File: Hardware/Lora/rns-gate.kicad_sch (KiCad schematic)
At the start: 2 parts, among them J2 Conn_02x13_Odd_Even, U1 E22-900M30S-SX1262

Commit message: Update Lora module
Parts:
- added C1: C_Polarized_Small, Capacitor_Tantalum_SMD:CP_EIA-7343-43_Kemet-X_Pad2.25x2.55mm_HandSolder, symbol Device:C_Polarized_Small
- added C2, C3: C_Small, Capacitor_SMD:C_0805_2012Metric_Pad1.18x1.45mm_HandSolder, symbol Device:C_Small
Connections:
- net +5V: now also C1.1, C2.1, C3.1
- net GND: now also C1.2, C2.2, C3.2
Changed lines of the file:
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@@
 (kicad_sch (version 20211123) (generator eeschema)
   (paper "A4")
+  (junction (at 144.78 159.004) (diameter 0) (color 0 0 0 0)
+  )
+  (junction (at 144.78 169.418) (diameter 0) (color 0 0 0 0)
+  )
+  (junction (at 152.654 159.004) (diameter 0) (color 0 0 0 0)
+  )
   (junction (at 160.02 144.018) (diameter 0) (color 0 0 0 0)
+  )
+  (junction (at 152.654 169.418) (diameter 0) (color 0 0 0 0)
   )
   (no_connect (at 106.172 119.888))
@@
   (no_connect (at 163.576 116.078))
   (no_connect (at 163.576 136.398))
+  (wire (pts (xy 144.78 169.418) (xy 152.654 169.418))
+    (stroke (width 0) (type default) (color 0 0 0 0))
+  )
   (wire (pts (xy 176.276 138.938) (xy 182.372 138.938))
     (stroke (width 0) (type default) (color 0 0 0 0))
   )
+  (wire (pts (xy 161.29 166.37) (xy 161.29 169.418))
+    (stroke (width 0) (type default) (color 0 0 0 0))
+  )
   (wire (pts (xy 156.718 128.778) (xy 163.576 128.778))
     (stroke (width 0) (type default) (color 0 0 0 0))
@@
     (stroke (width 0) (type default) (color 0 0 0 0))
   )
+  (wire (pts (xy 152.654 159.004) (xy 161.29 159.004))
+    (stroke (width 0) (type default) (color 0 0 0 0))
+  )
+  (wire (pts (xy 144.78 159.004) (xy 144.78 161.29))
+    (stroke (width 0) (type default) (color 0 0 0 0))
+  )
   (wire (pts (xy 176.276 121.158) (xy 181.61 121.158))
     (stroke (width 0) (type default) (color 0 0 0 0))
@@
     (stroke (width 0) (type default) (color 0 0 0 0))
   )
+  (wire (pts (xy 144.78 156.972) (xy 144.78 159.004))
+    (stroke (width 0) (type default) (color 0 0 0 0))
+  )
   (wire (pts (xy 155.448 141.478) (xy 163.576 141.478))
     (stroke (width 0) (type default) (color 0 0 0 0))
@@
     (stroke (width 0) (type default) (color 0 0 0 0))
   )
+  (wire (pts (xy 144.78 169.418) (xy 144.78 171.196))
+    (stroke (width 0) (type default) (color 0 0 0 0))
+  )
   (wire (pts (xy 176.276 141.478) (xy 182.372 141.478))
     (stroke (width 0) (type default) (color 0 0 0 0))
@@
     (stroke (width 0) (type default) (color 0 0 0 0))
   )
+  (wire (pts (xy 152.654 159.004) (xy 152.654 161.29))
+    (stroke (width 0) (type default) (color 0 0 0 0))
+  )
   (wire (pts (xy 176.276 118.618) (xy 181.61 118.618))
     (stroke (width 0) (type default) (color 0 0 0 0))
@@
     (stroke (width 0) (type default) (color 0 0 0 0))
   )
+  (wire (pts (xy 152.654 169.418) (xy 161.29 169.418))
+    (stroke (width 0) (type default) (color 0 0 0 0))
+  )
   (wire (pts (xy 156.718 121.158) (xy 163.576 121.158))
     (stroke (width 0) (type default) (color 0 0 0 0))
   )
+  (wire (pts (xy 144.78 166.37) (xy 144.78 169.418))
+    (stroke (width 0) (type default) (color 0 0 0 0))
+  )
+  (wire (pts (xy 161.29 159.004) (xy 161.29 161.29))
+    (stroke (width 0) (type default) (color 0 0 0 0))
+  )
   (wire (pts (xy 71.12 130.048) (xy 80.772 130.048))
     (stroke (width 0) (type default) (color 0 0 0 0))
@@
   )
   (wire (pts (xy 71.12 142.748) (xy 80.772 142.748))
+    (stroke (width 0) (type default) (color 0 0 0 0))
+  )
+  (wire (pts (xy 144.78 159.004) (xy 152.654 159.004))
+    (stroke (width 0) (type default) (color 0 0 0 0))
+  )
+  (wire (pts (xy 152.654 166.37) (xy 152.654 169.418))
     (stroke (width 0) (type default) (color 0 0 0 0))
   )
@@
     )
     (property "Datasheet" "" (id 3) (at 93.472 109.22 0)
+      (effects (font (size 1.27 1.27)) hide)
+    )
+    (pin "1")
+  )
+  (symbol (lib_id "power:GND") (at 144.78 171.196 0) (mirror y) (unit 1)
+    (in_bom yes) (on_board yes)
+    (property "Reference" "#PWR0107" (id 0) (at 144.78 177.546 0)
+      (effects (font (size 1.27 1.27)) hide)
+    )
+    (property "Value" "GND" (id 1) (at 144.78 179.07 90)
+      (effects (font (size 1.27 1.27)) (justify left))
+    )
+    (property "Footprint" "" (id 2) (at 144.78 171.196 0)
+      (effects (font (size 1.27 1.27)) hide)
+    )
+    (property "Datasheet" "" (id 3) (at 144.78 171.196 0)
       (effects (font (size 1.27 1.27)) hide)
     )
@@
     (pin "9")
   )
+  (symbol (lib_id "power:+5V") (at 144.78 156.972 0) (unit 1)
+    (in_bom yes) (on_board yes)
+    (property "Reference" "#PWR0106" (id 0) (at 144.78 160.782 0)
+      (effects (font (size 1.27 1.27)) hide)
+    )
+    (property "Value" "+5V" (id 1) (at 144.78 148.844 90)
+      (effects (font (size 1.27 1.27)) (justify right))
+    )
+    (property "Footprint" "" (id 2) (at 144.78 156.972 0)
+      (effects (font (size 1.27 1.27)) hide)
+    )
+    (property "Datasheet" "" (id 3) (at 144.78 156.972 0)
+      (effects (font (size 1.27 1.27)) hide)
+    )
+    (pin "1")
+  )
+  (symbol (lib_id "Device:C_Small") (at 161.29 163.83 0) (unit 1)
+    (in_bom yes) (on_board yes) (fields_autoplaced)
+    (property "Reference" "C3" (id 0) (at 163.83 163.8362 0)
+      (effects (font (size 1.27 1.27)) (justify left))
+    )
+    (property "Value" "C_Small" (id 1) (at 163.83 165.1062 0)
+      (effects (font (size 1.27 1.27)) (justify left) hide)
+    )
+    (property "Footprint" "Capacitor_SMD:C_0805_2012Metric_Pad1.18x1.45mm_HandSolder" (id 2) (at 161.29 163.83 0)
+      (effects (font (size 1.27 1.27)) hide)
+    )
+    (property "Datasheet" "~" (id 3) (at 161.29 163.83 0)
+      (effects (font (size 1.27 1.27)) hide)
+    )
+    (pin "1")
+    (pin "2")
+  )
   (symbol (lib_id "power:GND") (at 93.472 153.67 0) (unit 1)
     (in_bom yes) (on_board yes) (fields_autoplaced)
@@
     )
     (pin "1")
+  )
+  (symbol (lib_id "Device:C_Small") (at 152.654 163.83 0) (unit 1)
+    (in_bom yes) (on_board yes)
+    (property "Reference" "C2" (id 0) (at 155.702 163.83 0)
+      (effects (font (size 1.27 1.27)) (justify left))
+    )
+    (property "Value" "C_Small" (id 1) (at 155.194 165.1062 0)
+      (effects (font (size 1.27 1.27)) (justify left) hide)
+    )
+    (property "Footprint" "Capacitor_SMD:C_0805_2012Metric_Pad1.18x1.45mm_HandSolder" (id 2) (at 152.654 163.83 0)
+      (effects (font (size 1.27 1.27)) hide)
+    )
+    (property "Datasheet" "~" (id 3) (at 152.654 163.83 0)
+      (effects (font (size 1.27 1.27)) hide)
+    )
+    (pin "1")
+    (pin "2")
   )
   (symbol (lib_id "Connector_Generic:Conn_02x13_Odd_Even") (at 171.196 131.318 180) (unit 1)
@@
     (pin "1")
   )
+  (symbol (lib_id "Device:C_Polarized_Small") (at 144.78 163.83 0) (unit 1)
+    (in_bom yes) (on_board yes)
+    (property "Reference" "C1" (id 0) (at 147.066 163.83 0)
+      (effects (font (size 1.27 1.27)) (justify left))
+    )
+    (property "Value" "C_Polarized_Small" (id 1) (at 147.574 164.5538 0)
+      (effects (font (size 1.27 1.27)) (justify left) hide)
+    )
+    (property "Footprint" "Capacitor_Tantalum_SMD:CP_EIA-7343-43_Kemet-X_Pad2.25x2.55mm_HandSolder" (id 2) (at 144.78 163.83 0)
+      (effects (font (size 1.27 1.27)) hide)
+    )
+    (property "Datasheet" "~" (id 3) (at 144.78 163.83 0)
+      (effects (font (size 1.27 1.27)) hide)
+    )
+    (pin "1")
+    (pin "2")
+  )
   (sheet_instances
     (path "/" (page "1"))
@@
       (reference "#PWR0105") (unit 1) (value "+5V") (footprint "")
     )
+    (path "/2cf41d00-cacc-4dad-9843-7bad44532c96"
+      (reference "#PWR0106") (unit 1) (value "+5V") (footprint "")
+    )
+    (path "/1cf30780-29ec-420e-a6ba-e2a0a07a3fff"
+      (reference "#PWR0107") (unit 1) (value "GND") (footprint "")
+    )
+    (path "/eb54723c-0889-4ff8-b6b9-90a29929eabb"
+      (reference "C1") (unit 1) (value "C_Polarized_Small") (footprint "Capacitor_Tantalum_SMD:CP_EIA-7343-43_Kemet-X_Pad2.25x2.55mm_HandSolder")
+    )
+    (path "/63f30bb4-b6ba-46dc-b320-d16f9c4787c9"
+      (reference "C2") (unit 1) (value "C_Small") (footprint "Capacitor_SMD:C_0805_2012Metric_Pad1.18x1.45mm_HandSolder")
+    )
+    (path "/2e3fd31c-7d58-4b3e-91bd-5d4203af8081"
+      (reference "C3") (unit 1) (value "C_Small") (footprint "Capacitor_SMD:C_0805_2012Metric_Pad1.18x1.45mm_HandSolder")
+    )
     (path "/67dc5d05-0267-48c8-80ec-d8ee74f8beba"

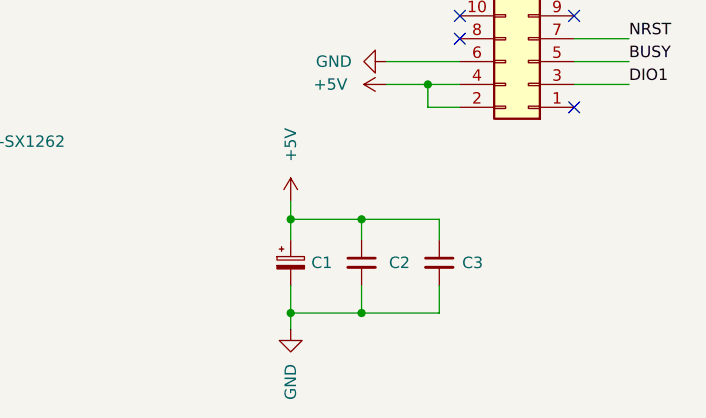
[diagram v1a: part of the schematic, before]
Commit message: Update Lora schematic
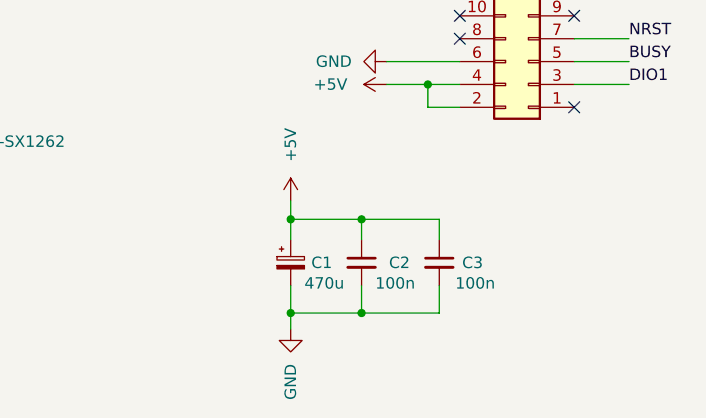
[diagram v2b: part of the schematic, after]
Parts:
- C1: value C_Polarized_Small -> 470u
- C2, C3: value C_Small -> 100n
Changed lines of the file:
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@@
   )
   (symbol (lib_id "Device:C_Small") (at 161.29 163.83 0) (unit 1)
-    (in_bom yes) (on_board yes) (fields_autoplaced)
+    (in_bom yes) (on_board yes)
     (property "Reference" "C3" (id 0) (at 163.83 163.8362 0)
       (effects (font (size 1.27 1.27)) (justify left))
     )
-    (property "Value" "C_Small" (id 1) (at 163.83 165.1062 0)
-      (effects (font (size 1.27 1.27)) (justify left) hide)
+    (property "Value" "100n" (id 1) (at 163.068 166.116 0)
+      (effects (font (size 1.27 1.27)) (justify left))
     )
     (property "Footprint" "Capacitor_SMD:C_0805_2012Metric_Pad1.18x1.45mm_HandSolder" (id 2) (at 161.29 163.83 0)
@@
       (effects (font (size 1.27 1.27)) (justify left))
     )
-    (property "Value" "C_Small" (id 1) (at 155.194 165.1062 0)
-      (effects (font (size 1.27 1.27)) (justify left) hide)
+    (property "Value" "100n" (id 1) (at 154.178 166.116 0)
+      (effects (font (size 1.27 1.27)) (justify left))
     )
     (property "Footprint" "Capacitor_SMD:C_0805_2012Metric_Pad1.18x1.45mm_HandSolder" (id 2) (at 152.654 163.83 0)
@@
       (effects (font (size 1.27 1.27)) (justify left))
     )
-    (property "Value" "C_Polarized_Small" (id 1) (at 147.574 164.5538 0)
-      (effects (font (size 1.27 1.27)) (justify left) hide)
+    (property "Value" "470u" (id 1) (at 146.304 166.116 0)
+      (effects (font (size 1.27 1.27)) (justify left))
     )
     (property "Footprint" "Capacitor_Tantalum_SMD:CP_EIA-7343-43_Kemet-X_Pad2.25x2.55mm_HandSolder" (id 2) (at 144.78 163.83 0)
@@
     )
     (path "/eb54723c-0889-4ff8-b6b9-90a29929eabb"
-      (reference "C1") (unit 1) (value "C_Polarized_Small") (footprint "Capacitor_Tantalum_SMD:CP_EIA-7343-43_Kemet-X_Pad2.25x2.55mm_HandSolder")
+      (reference "C1") (unit 1) (value "470u") (footprint "Capacitor_Tantalum_SMD:CP_EIA-7343-43_Kemet-X_Pad2.25x2.55mm_HandSolder")
     )
     (path "/63f30bb4-b6ba-46dc-b320-d16f9c4787c9"
-      (reference "C2") (unit 1) (value "C_Small") (footprint "Capacitor_SMD:C_0805_2012Metric_Pad1.18x1.45mm_HandSolder")
+      (reference "C2") (unit 1) (value "100n") (footprint "Capacitor_SMD:C_0805_2012Metric_Pad1.18x1.45mm_HandSolder")
     )
     (path "/2e3fd31c-7d58-4b3e-91bd-5d4203af8081"
-      (reference "C3") (unit 1) (value "C_Small") (footprint "Capacitor_SMD:C_0805_2012Metric_Pad1.18x1.45mm_HandSolder")
+      (reference "C3") (unit 1) (value "100n") (footprint "Capacitor_SMD:C_0805_2012Metric_Pad1.18x1.45mm_HandSolder")
     )
     (path "/67dc5d05-0267-48c8-80ec-d8ee74f8beba"
